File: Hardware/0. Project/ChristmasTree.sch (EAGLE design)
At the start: 28 parts, among them CN1 CELL, CN2 Micro USB Type B, IC1 ATMEGA32U4-MU, U1 RT9193-33GB, Y1 8MHz

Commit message: WIP
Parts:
- removed C14: 1uF, microbuilder:CAP_CERAMIC0603_NO
- removed C9: 10uF, microbuilder:CAP_CERAMIC0805-NOOUTLINE
- removed IC1: ATMEGA32U4-MU, microbuilder:ATMEGA32U4-MU
- added C2, C8: 1uF, My-RLC:C_0603
- added C3, C4, C5, C7: 100nF, My-RLC:C_0603
- added C6: 10uF, My-RLC:C_0805
- added R9: 10k (5%), My-RLC:R_0603
- added U3: ATMEGA32U4, SparkFun_Pro_Micro_v13a:TESTING_ATMEGA32U4QFN
- R4, R5: value 22R -> 22R (5%)
- Y1: device SparkFun:RESONATORSMD -> crystal2:CRYSTALHC49UP
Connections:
- removed net +3V3: C9.1, IC1.AVCC, IC1.AVCC1, IC1.PE2(!HWB), IC1.UCAP, IC1.VCC, IC1.VCC1
- removed net A0: IC1.PF7(ADC7(TDI)
- removed net A1: IC1.PF6(ADC6/TDO)
- removed net A2: IC1.PF5(ADC5/TMS)
- removed net A3: IC1.PF4(ADC4/TCK)
- removed net A4: IC1.PF1(ADC1)
- removed net A5: IC1.PF0(ADC0)
- removed net AREF: C14.1, IC1.AREF
- removed net D0: IC1.PD2(INT2/RXD1)
- removed net D1: IC1.PD3(INT3/TXD1)
- removed net D10: IC1.PB6(OC1B/OC4B/ADC13)
- removed net D11: IC1.PB7(OC0A/OC1C/RTS)
- removed net D12: IC1.PD6(T1/ADC9/!OC4D)
- removed net D13: IC1.PC7(ICP3/CLK0/OC4A)
- removed net D4: IC1.PD4(ICP1/ADC8)
- removed net D5: IC1.PC6(OC3A/!OC4A)
- removed net D6: IC1.PD7(OC4D/ADC10/T0)
- removed net D7: IC1.PE6(INT.6/AIN0)
- removed net D8: IC1.PB4(ADC11)
- removed net D9: IC1.PB5(OC1A/ADC12/!OC4B)
- removed net GND: C14.2, C9.2, IC1.GND, IC1.GND1, IC1.GND2, IC1.GND3, IC1.UGND, Y1.2
- removed net MISO: IC1.PB3(PDO/MISO)
- removed net MOSI: IC1.PB2(PDI/MOSI)
- removed net RST: IC1./RESET
- removed net SCK: IC1.PB1(SCK)
- removed net SCL: IC1.PD0(INT0/OC0B/SCL)
- removed net SDA: IC1.PD1(INT1/SDA)
- new net N$18: C7.1, U3.AREF
- new net N$19: U3.PD7(ADC10)
- new net P$1: U3.UVCC, U3.VBUS
- new net RESET: R9.1, U3.!RESET
- net 0V: now also C2.2, C3.2, C4.2, C5.2, C6.2, C7.2, C8.2, U3.GND@15, U3.GND@23, U3.GND@35, U3.GND@43, U3.PE2/!HWB, U3.UGND
- net 3.3V: now also C5.1, C8.1, R9.2, U3.AVCC@24, U3.AVCC@44, U3.VCC@14, U3.VCC@34
- net N$15: now also C3.1, U3.XTAL1, Y1.1; no longer IC1.XTAL2, Y1.3
- net N$16: now also C4.1, U3.XTAL2, Y1.2; no longer IC1.XTAL1, Y1.1
- net N$17: now also C2.1, U3.UCAP; no longer CN2G$1.1, D3.A
- net USB_D+: now also U3.D+; no longer IC1.D+
- net USB_D-: now also U3.D-; no longer IC1.D-
- net VBUS: now also C6.1, CN2G$1.1, D3.A; no longer IC1.VBUS
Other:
- moved on the sheet: C1, D3, R4, R5

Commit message: PCB 100mm
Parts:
- removed D3: SS34, My-Diodes:SS34
- removed R9: 10k (5%), My-RLC:R_0603
- removed U3: ATMEGA32U4, SparkFun_Pro_Micro_v13a:TESTING_ATMEGA32U4QFN
- added D1: SS34, My-Diodes:SS34
- added LDR1: A1050_09, photo-elements:A1050_09
- added R1: 10k (5%), My-RLC:R_0603
- added R3: 22R (5%), My-RLC:R_0603
- added U2: ATMEGA32U4, SparkFun_Pro_Micro_v13a:TESTING_ATMEGA32U4QFN
- C1: value 22nF -> 10uF; device My-RLC:C_0603 -> My-RLC:C_0805
- C2: value 1uF -> 22nF
- C3, C5: value 100nF -> 1uF
- C6: value 10uF -> 100nF; device My-RLC:C_0805 -> My-RLC:C_0603
- C8: value 1uF -> 100nF
- CN1: value CELL -> Micro USB Type B; device My-Battery:CELL -> My-Connectors:MICRO-USB
- CN2: value Micro USB Type B -> CELL; device My-Connectors:MICRO-USB -> My-Battery:CELL
- R2: value 470R -> 22R (5%); device rcl:R-EU_R0603 -> My-RLC:R_0603
- R4: value 22R (5%) -> 470R; device My-RLC:R_0603 -> rcl:R-EU_R0603
- R5: value 22R (5%) -> 10k (5%)
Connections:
- removed net N$20: CN2G$1.2, R4.1
- removed net N$23: CN2G$1.3, R5.1
- removed net N$24: CN1.+, D2.A, SJ1.1
- removed net P$1: U3.UVCC, U3.VBUS
- new net LEDS_CONTROL: LED1.DI, R4.2
- new net LIGHT_SENSOR: LDR1.2, R5.2, U2.PF7(ADC7)
- net 0V: now also CN1G$1.5, CN1G$2.S1, CN1G$2.S2, CN1G$2.S3, CN1G$2.S4, CN2.-, R5.1, U2.GND@15, U2.GND@23, U2.GND@35, U2.GND@43, U2.PE2/!HWB, U2.UGND; no longer CN1.-, CN2G$1.5, CN2G$2.S1, CN2G$2.S2, CN2G$2.S3, CN2G$2.S4, U3.GND@15, U3.GND@23, U3.GND@35, U3.GND@43, U3.PE2/!HWB, U3.UGND
- net 3.3V: now also C3.1, C4.1, LDR1.1, R1.2, U2.AVCC@24, U2.AVCC@44, U2.VCC@14, U2.VCC@34; no longer C5.1, C8.1, R9.2, U3.AVCC@24, U3.AVCC@44, U3.VCC@14, U3.VCC@34
- net N$11: now also LED4.DO; no longer LED2.DO
- net N$15: now also C7.1, U2.XTAL1; no longer C3.1, U3.XTAL1
- net N$16: now also C8.1, U2.XTAL2; no longer C4.1, U3.XTAL2
- net N$17: now also C5.1, U2.UCAP; no longer C2.1, U3.UCAP
- net N$18: now also C6.1, U2.AREF; no longer C7.1, U3.AREF
- net N$19: now also CN2.+, D2.A, SJ1.1; no longer U3.PD7(ADC10)
- net N$21: now also C2.1; no longer C1.1
- net N$3: now also R4.1, U2.PD7(ADC10); no longer LED3.DI, R2.2
- net N$4: now also LED2.DO, LED3.DI; no longer LED1.DI, LED4.DO
- net RESET: now also R1.1, U2.!RESET; no longer R9.1, U3.!RESET
- net USB_D+: now also CN1G$1.3, R3.1, R3.2, U2.D+; no longer R5.2, U3.D+
- net USB_D-: now also CN1G$1.2, R2.1, R2.2, U2.D-; no longer R4.2, U3.D-
- net VBAT: now also D1.K; no longer D3.K
- net VBUS: now also C1.1, CN1G$1.1, D1.A, U2.UVCC, U2.VBUS; no longer C6.1, CN2G$1.1, D3.A
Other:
- moved on the sheet: C1, C2, C3, C4, C5, C6, C7, C8, D2, LED1, LED10, LED11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

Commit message: WIP
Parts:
- removed LED14: WS2812B, My-LED:WS2812B
- added TP1, TP2: TPSQTP20R, testpad:TPSQTP20R
- CN2: value CELL -> 3.7V; device My-Battery:CELL -> My-Battery:CELL-CONNECTOR
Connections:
- removed net N$12: LED13.DO, LED14.DI
- net 0V: no longer LED14.GND
- net 3.3V: no longer LED14.VDD
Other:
- moved on the sheet: C1, C2, C3, C4, C5, C6, C7, C8, CN1, CN2, D1, D2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

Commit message: PCB 1.0 done
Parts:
- removed TP1, TP2: TPSQTP20R, testpad:TPSQTP20R
- added C10, C11, C12, C13, C14, C15, C16, C17, C18, C19, C20, C21, C9: 100nF, My-RLC:C_0603
- added MH1, MH2: TPSQTP20R, testpad:TPSQTP20R
- R4: device rcl:R-EU_R0603 -> My-RLC:R_0603
- Y1: device crystal2:CRYSTALHC49UP -> crystal-geyer_V1_0:KX-9A
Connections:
- new net N$12: R3.2, U2.D+
- new net N$20: R2.2, U2.D-
- net 0V: now also C10.2, C11.2, C12.2, C13.2, C14.2, C15.2, C16.2, C17.2, C18.2, C19.2, C20.2, C21.2, C9.2
- net 3.3V: now also C10.1, C11.1, C12.1, C13.1, C14.1, C15.1, C16.1, C17.1, C18.1, C19.1, C20.1, C21.1, C9.1
- net USB_D+: no longer R3.2, U2.D+
- net USB_D-: no longer R2.2, U2.D-
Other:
- note added: "."
- moved on the sheet: LDR1

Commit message: Basic firmware test
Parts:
- R5: value 10k (5%) -> 100k (5%)
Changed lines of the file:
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@@
 <part name="SUPPLY47" library="My-Supply" deviceset="0V" device=""/>
 <part name="SUPPLY48" library="My-Supply" deviceset="0V" device=""/>
-<part name="LDR1" library="photo-elements" deviceset="A10" device="" package3d_urn="urn:adsk.eagle:package:23501050/2" override_package3d_urn="urn:adsk.eagle:package:23536266/2" override_package_urn="urn:adsk.eagle:footprint:23536267/1" technology="50_09" value="A1050_09"/>
+<part name="LDR1" library="photo-elements" deviceset="A10" device="" package3d_urn="urn:adsk.eagle:package:23501050/2" override_package3d_urn="urn:adsk.eagle:package:23536266/2" override_package_urn="urn:adsk.eagle:footprint:23536267/1" technology="50_09" value=""/>
 <part name="SUPPLY33" library="My-Supply" deviceset="3.3V" device=""/>
-<part name="R5" library="My-RLC" deviceset="R_" device="0603" package3d_urn="urn:adsk.eagle:package:23494030/2" value="10k (5%)"/>
+<part name="R5" library="My-RLC" deviceset="R_" device="0603" package3d_urn="urn:adsk.eagle:package:23494030/2" value="100k (5%)"/>
 <part name="SUPPLY34" library="My-Supply" deviceset="0V" device=""/>
 <part name="MH1" library="testpad" library_urn="urn:adsk.eagle:library:385" deviceset="TPSQ" device="TP20R" package3d_urn="urn:adsk.eagle:package:27973/1"/>

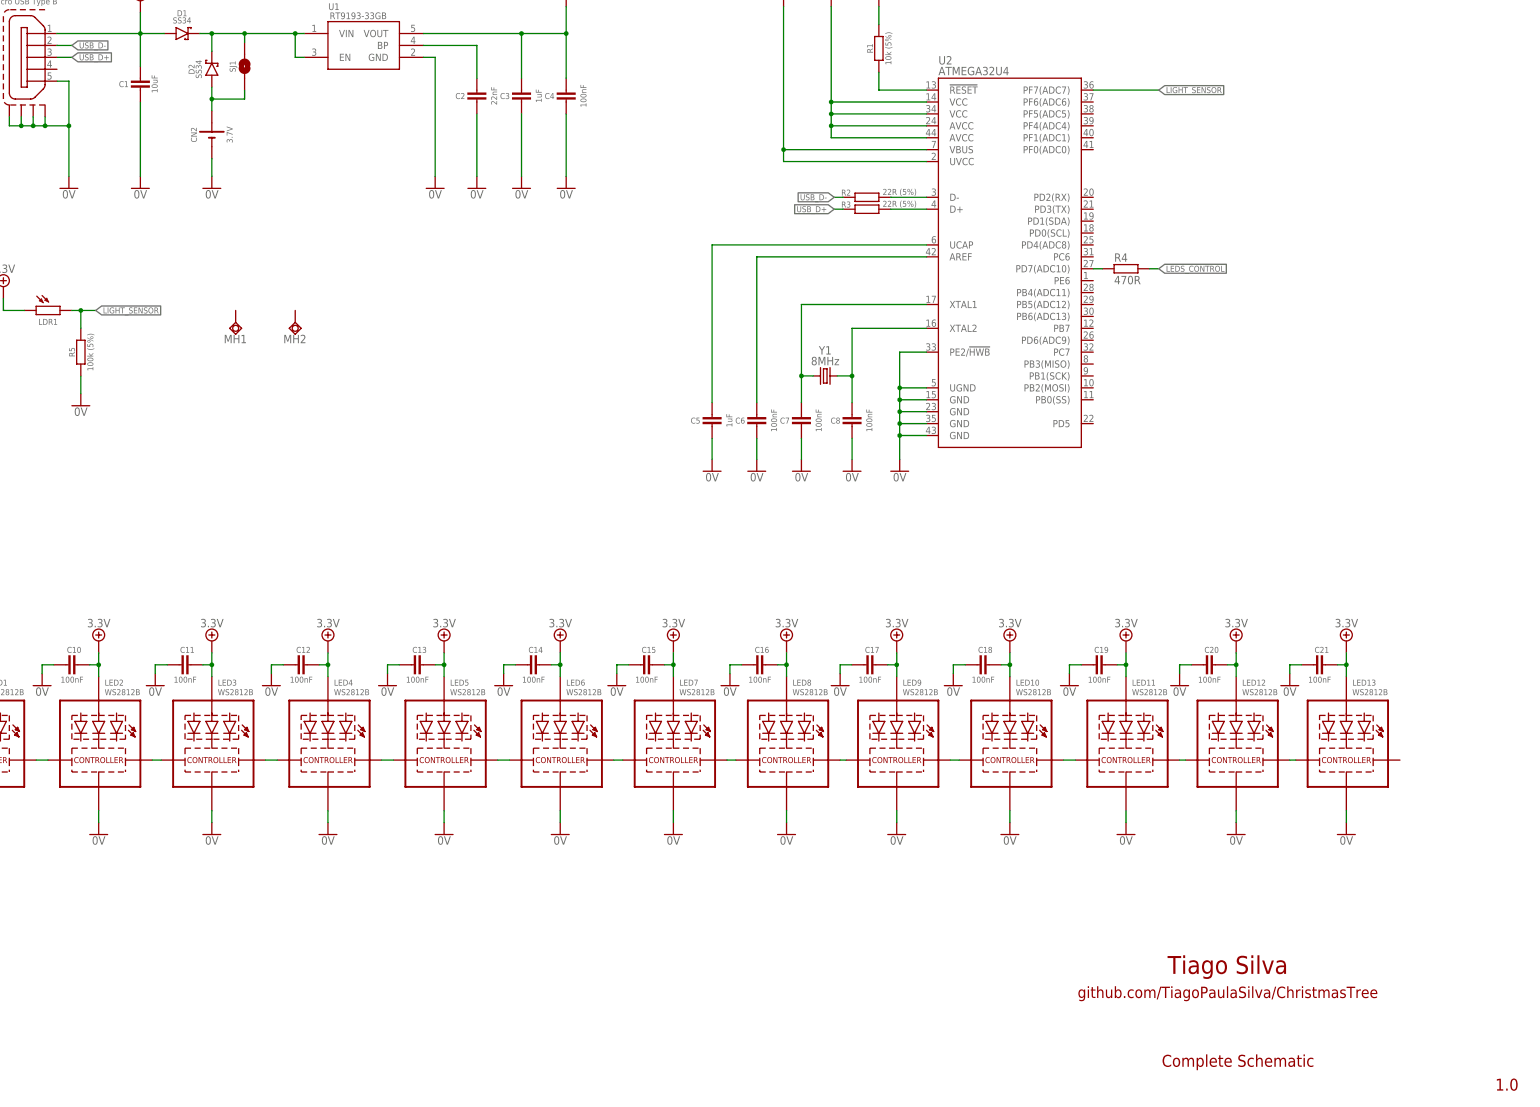
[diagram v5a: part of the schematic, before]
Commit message: Adequacy of values in some components
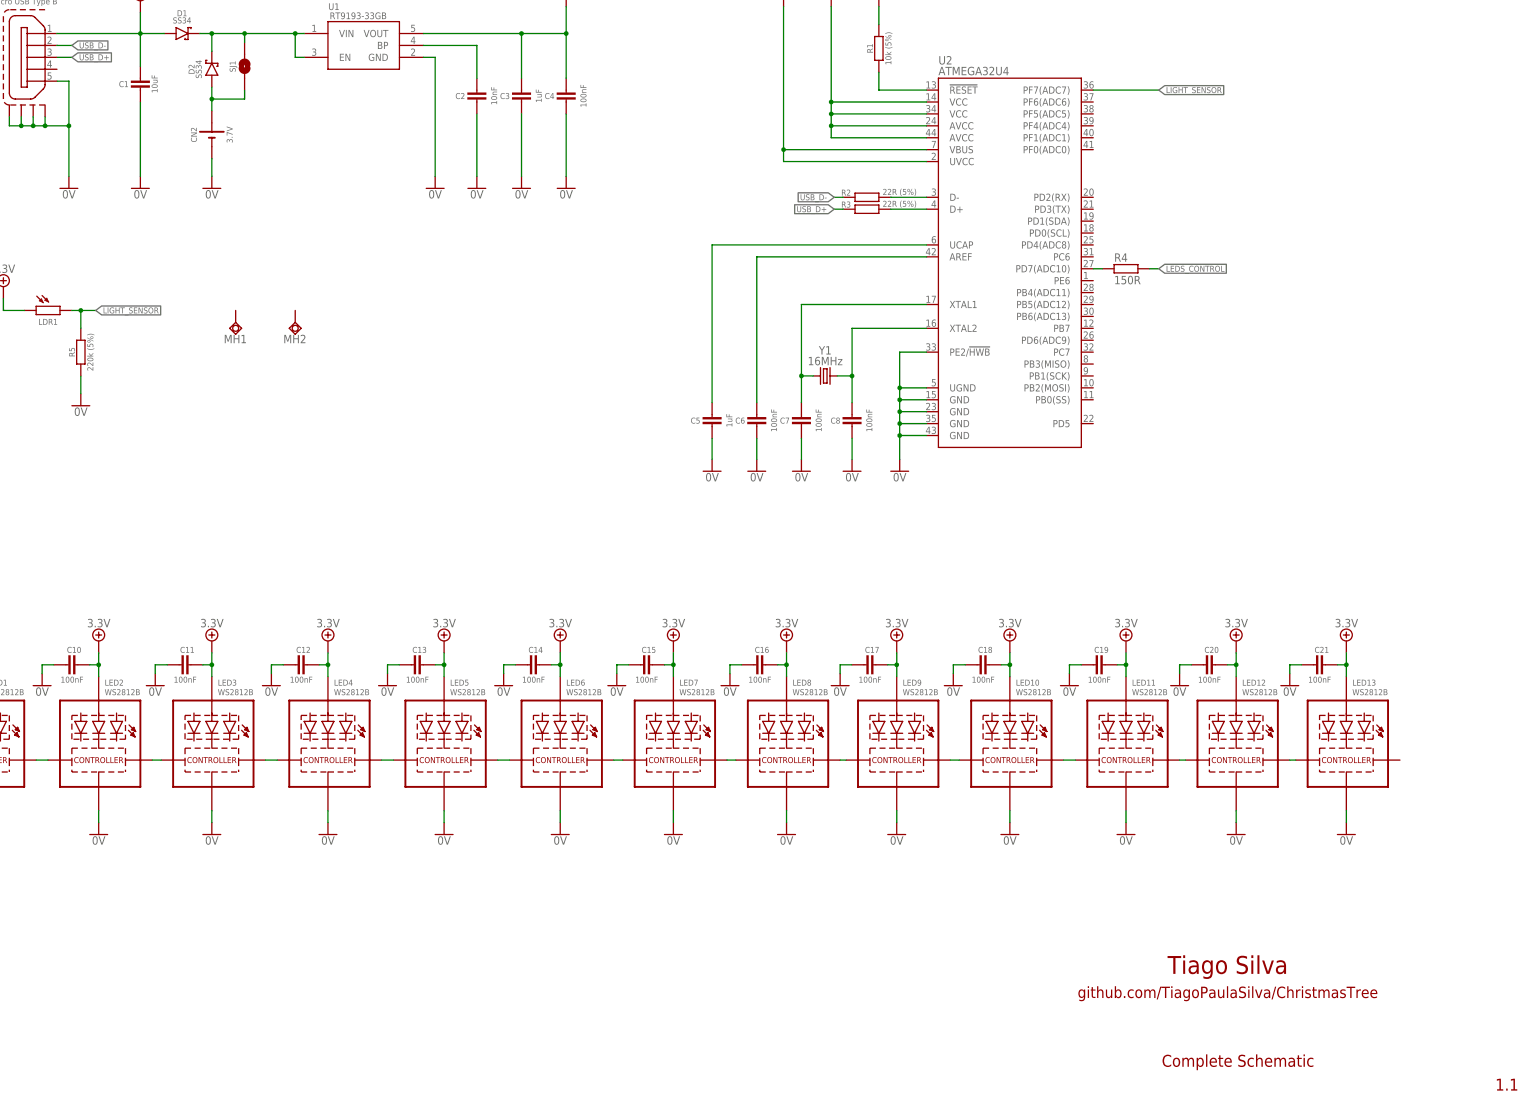
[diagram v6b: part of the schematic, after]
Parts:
- C2: value 22nF -> 10nF
- R4: value 470R -> 150R
- R5: value 100k (5%) -> 220k (5%)
- Y1: value 8MHz -> 16MHz
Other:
- note added: "*"
- note added: "1.1"
- note added: "SJ1 OPEN while working on the firmware CLOSE while in normal operation"
- note removed: "1.0"
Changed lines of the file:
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@@
 <part name="LED1" library="My-LED" deviceset="WS2812B" device="" package3d_urn="urn:adsk.eagle:package:23501017/2"/>
 <part name="LED2" library="My-LED" deviceset="WS2812B" device="" package3d_urn="urn:adsk.eagle:package:23501017/2"/>
-<part name="R4" library="My-RLC" deviceset="R_" device="0603" package3d_urn="urn:adsk.eagle:package:23494030/2" value="470R"/>
+<part name="R4" library="My-RLC" deviceset="R_" device="0603" package3d_urn="urn:adsk.eagle:package:23494030/2" value="150R"/>
 <part name="SUPPLY1" library="My-Supply" deviceset="0V" device=""/>
 <part name="SUPPLY2" library="My-Supply" deviceset="0V" device=""/>
@@
 <part name="U1" library="RT9193-33GB" deviceset="RT9193-33GB" device="" package3d_urn="urn:adsk.eagle:package:23536219/2"/>
 <part name="D2" library="My-Diodes" deviceset="SS34" device="" package3d_urn="urn:adsk.eagle:package:23536213/2"/>
-<part name="C2" library="My-RLC" deviceset="C_" device="0603" package3d_urn="urn:adsk.eagle:package:23494015/2" value="22nF"/>
+<part name="C2" library="My-RLC" deviceset="C_" device="0603" package3d_urn="urn:adsk.eagle:package:23494015/2" value="10nF"/>
 <part name="SUPPLY29" library="My-Supply" deviceset="0V" device=""/>
 <part name="SUPPLY30" library="My-Supply" deviceset="0V" device=""/>
@@
 <part name="SUPPLY42" library="My-Supply" deviceset="0V" device=""/>
 <part name="SUPPLY44" library="My-Supply" deviceset="0V" device=""/>
-<part name="Y1" library="crystal-geyer_V1_0" library_urn="urn:adsk.eagle:library:203" deviceset="KX" device="-9A" package3d_urn="urn:adsk.eagle:package:11927/1" override_package3d_urn="urn:adsk.eagle:package:23536242/2" override_package_urn="urn:adsk.eagle:footprint:11874/1" value="8MHz"/>
+<part name="Y1" library="crystal-geyer_V1_0" library_urn="urn:adsk.eagle:library:203" deviceset="KX" device="-9A" package3d_urn="urn:adsk.eagle:package:11927/1" override_package3d_urn="urn:adsk.eagle:package:23536242/2" override_package_urn="urn:adsk.eagle:footprint:11874/1" value="16MHz"/>
 <part name="C7" library="My-RLC" deviceset="C_" device="0603" package3d_urn="urn:adsk.eagle:package:23494015/2" value="100nF"/>
 <part name="C8" library="My-RLC" deviceset="C_" device="0603" package3d_urn="urn:adsk.eagle:package:23494015/2" value="100nF"/>
@@
 <part name="LDR1" library="photo-elements" deviceset="A10" device="" package3d_urn="urn:adsk.eagle:package:23501050/2" override_package3d_urn="urn:adsk.eagle:package:23536266/2" override_package_urn="urn:adsk.eagle:footprint:23536267/1" technology="50_09" value=""/>
 <part name="SUPPLY33" library="My-Supply" deviceset="3.3V" device=""/>
-<part name="R5" library="My-RLC" deviceset="R_" device="0603" package3d_urn="urn:adsk.eagle:package:23494030/2" value="100k (5%)"/>
+<part name="R5" library="My-RLC" deviceset="R_" device="0603" package3d_urn="urn:adsk.eagle:package:23494030/2" value="220k (5%)"/>
 <part name="SUPPLY34" library="My-Supply" deviceset="0V" device=""/>
 <part name="MH1" library="testpad" library_urn="urn:adsk.eagle:library:385" deviceset="TPSQ" device="TP20R" package3d_urn="urn:adsk.eagle:package:27973/1"/>
@@
 <text x="320.802" y="28.067" size="3.81" layer="94" align="center">Tiago Silva</text>
 <text x="320.802" y="22.225" size="2.413" layer="94" align="center">github.com/TiagoPaulaSilva/ChristmasTree</text>
-<text x="377.825" y="1.27" size="2.54" layer="94" ratio="5">1.0</text>
+<text x="377.825" y="1.27" size="2.54" layer="94" ratio="5">1.1</text>
 <text x="306.705" y="6.35" size="2.54" layer="94" ratio="5">Complete Schematic</text>
 <text x="116.84" y="144.78" size="0.002540625" layer="97" ratio="0" grouprefs="MECHANICALS_SUPPORT">.</text>
 <text x="116.84" y="177.8" size="0.002540625" layer="97" ratio="0" grouprefs="MECHANICALS_SUPPORT">.</text>
+<text x="124.46" y="209.804" size="1.27" layer="98" font="vector" align="center">SJ1
+OPEN while working on the firmware
+CLOSE while in normal operation</text>
+<text x="114.554" y="219.964" size="5.08" layer="98" font="vector" align="center">*</text>
+<text x="121.158" y="213.36" size="5.08" layer="98" font="vector" align="center">*</text>
 </plain>
 <instances>
@@
 </drawing>
 <compatibility>
+<note version="6.3" minversion="6.2.2" severity="warning">
+Since Version 6.2.2 text objects can contain more than one line,
+which will not be processed correctly with this version.
+</note>
 <note version="8.2" severity="warning">
 Since Version 8.2, EAGLE supports online libraries. The ids
